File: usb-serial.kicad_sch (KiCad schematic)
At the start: 29 parts, among them J11 Connector, USB-TYPE-C-16P, J3 Connector, USB-TYPE-C-16P, Q8 L8050QLT1G, Q9 L8050QLT1G, U6 CP2102N-Axx-xQFN28

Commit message: fix: corrected 3v3 connections at D5, USB power to LDO, power to I2C expansion
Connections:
- net USB_5V is gone; now on net +5V: C11.1, D5.1 (K)
- net USB2_5V renamed +5V
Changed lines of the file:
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@@
 	(wire
 		(pts
-			(xy 119.38 104.14) (xy 119.38 107.95)
+			(xy 119.38 102.87) (xy 119.38 107.95)
 		)
 		(stroke
@@
 	)
 	(symbol
-		(lib_id "power:VBUS")
-		(at 120.65 34.29 0)
-		(unit 1)
-		(body_style 1)
-		(exclude_from_sim no)
-		(in_bom yes)
-		(on_board yes)
-		(in_pos_files yes)
-		(dnp no)
-		(fields_autoplaced yes)
-		(property "Reference" "#PWR050"
-			(at 120.65 38.1 0)
-			(hide yes)
-			(show_name no)
-			(do_not_autoplace no)
-			(effects
-				(font
-					(size 1.27 1.27)
-				)
-			)
-		)
-		(property "Value" "USB_5V"
-			(at 120.65 29.21 0)
-			(show_name no)
-			(do_not_autoplace no)
-			(effects
-				(font
-					(size 1.27 1.27)
-				)
-			)
-		)
-		(property "Footprint" ""
-			(at 120.65 34.29 0)
-			(hide yes)
-			(show_name no)
-			(do_not_autoplace no)
-			(effects
-				(font
-					(size 1.27 1.27)
-				)
-			)
-		)
-		(property "Datasheet" ""
-			(at 120.65 34.29 0)
-			(hide yes)
-			(show_name no)
-			(do_not_autoplace no)
-			(effects
-				(font
-					(size 1.27 1.27)
-				)
-			)
-		)
-		(property "Description" "Power symbol creates a global label with name \"VBUS\""
-			(at 120.65 34.29 0)
-			(hide yes)
-			(show_name no)
-			(do_not_autoplace no)
-			(effects
-				(font
-					(size 1.27 1.27)
-				)
-			)
-		)
-		(pin "1"
-		)
-		(instances
-			(project "presstimer"
-				(path "/63494a82-20b5-470b-977d-6a82bfa70174/0171fa45-2753-4764-a2d1-635868f3d686"
-					(reference "#PWR050")
-					(unit 1)
-				)
-			)
-		)
-	)
-	(symbol
 		(lib_id "PCM_JLCPCB-Extended:Connector, USB-TYPE-C-16P")
 		(at 43.18 53.34 0)
@@
 	)
 	(symbol
-		(lib_id "power:VBUS")
-		(at 119.38 104.14 0)
-		(unit 1)
-		(body_style 1)
-		(exclude_from_sim no)
-		(in_bom yes)
-		(on_board yes)
-		(in_pos_files yes)
-		(dnp no)
-		(fields_autoplaced yes)
-		(property "Reference" "#PWR062"
-			(at 119.38 107.95 0)
-			(hide yes)
-			(show_name no)
-			(do_not_autoplace no)
-			(effects
-				(font
-					(size 1.27 1.27)
-				)
-			)
-		)
-		(property "Value" "USB2_5V"
-			(at 119.38 99.06 0)
-			(show_name no)
-			(do_not_autoplace no)
-			(effects
-				(font
-					(size 1.27 1.27)
-				)
-			)
-		)
-		(property "Footprint" ""
-			(at 119.38 104.14 0)
-			(hide yes)
-			(show_name no)
-			(do_not_autoplace no)
-			(effects
-				(font
-					(size 1.27 1.27)
-				)
-			)
-		)
-		(property "Datasheet" ""
-			(at 119.38 104.14 0)
-			(hide yes)
-			(show_name no)
-			(do_not_autoplace no)
-			(effects
-				(font
-					(size 1.27 1.27)
-				)
-			)
-		)
-		(property "Description" "Power symbol creates a global label with name \"VBUS\""
-			(at 119.38 104.14 0)
-			(hide yes)
-			(show_name no)
-			(do_not_autoplace no)
-			(effects
-				(font
-					(size 1.27 1.27)
-				)
-			)
-		)
-		(pin "1"
-		)
-		(instances
-			(project "presstimer"
-				(path "/63494a82-20b5-470b-977d-6a82bfa70174/0171fa45-2753-4764-a2d1-635868f3d686"
-					(reference "#PWR062")
-					(unit 1)
-				)
-			)
-		)
-	)
-	(symbol
 		(lib_id "markus:1N5819HW-7-F")
 		(at 85.09 107.95 0)
@@
 	)
 	(symbol
+		(lib_id "power:+5V")
+		(at 120.65 34.29 0)
+		(unit 1)
+		(body_style 1)
+		(exclude_from_sim no)
+		(in_bom yes)
+		(on_board yes)
+		(in_pos_files yes)
+		(dnp no)
+		(fields_autoplaced yes)
+		(property "Reference" "#PWR018"
+			(at 120.65 38.1 0)
+			(hide yes)
+			(show_name no)
+			(do_not_autoplace no)
+			(effects
+				(font
+					(size 1.27 1.27)
+				)
+			)
+		)
+		(property "Value" "+5V"
+			(at 120.65 29.21 0)
+			(show_name no)
+			(do_not_autoplace no)
+			(effects
+				(font
+					(size 1.27 1.27)
+				)
+			)
+		)
+		(property "Footprint" ""
+			(at 120.65 34.29 0)
+			(hide yes)
+			(show_name no)
+			(do_not_autoplace no)
+			(effects
+				(font
+					(size 1.27 1.27)
+				)
+			)
+		)
+		(property "Datasheet" ""
+			(at 120.65 34.29 0)
+			(hide yes)
+			(show_name no)
+			(do_not_autoplace no)
+			(effects
+				(font
+					(size 1.27 1.27)
+				)
+			)
+		)
+		(property "Description" "Power symbol creates a global label with name \"+5V\""
+			(at 120.65 34.29 0)
+			(hide yes)
+			(show_name no)
+			(do_not_autoplace no)
+			(effects
+				(font
+					(size 1.27 1.27)
+				)
+			)
+		)
+		(pin "1"
+		)
+		(instances
+			(project "presstimer"
+				(path "/63494a82-20b5-470b-977d-6a82bfa70174/0171fa45-2753-4764-a2d1-635868f3d686"
+					(reference "#PWR018")
+					(unit 1)
+				)
+			)
+		)
+	)
+	(symbol
 		(lib_id "power:GND")
 		(at 223.52 123.19 0)
@@
 					(unit 1)
 				)
+			)
+		)
+	)
+	(symbol
+		(lib_id "power:+5V")
+		(at 119.38 102.87 0)
+		(unit 1)
+		(body_style 1)
+		(exclude_from_sim no)
+		(in_bom yes)
+		(on_board yes)
+		(in_pos_files yes)
+		(dnp no)
+		(fields_autoplaced yes)
+		(property "Reference" "#PWR019"
+			(at 119.38 106.68 0)
+			(hide yes)
+			(show_name no)
+			(do_not_autoplace no)
+			(effects
+				(font
+					(size 1.27 1.27)
+				)
+			)
+		)
+		(property "Value" "+5V"
+			(at 119.38 97.79 0)
+			(show_name no)
+			(do_not_autoplace no)
+			(effects
+				(font
+					(size 1.27 1.27)
+				)
+			)
+		)
+		(property "Footprint" ""
+			(at 119.38 102.87 0)
+			(hide yes)
+			(show_name no)
+			(do_not_autoplace no)
+			(effects
+				(font
+					(size 1.27 1.27)
+				)
+			)
+		)
+		(property "Datasheet" ""
+			(at 119.38 102.87 0)
+			(hide yes)
+			(show_name no)
+			(do_not_autoplace no)
+			(effects
+				(font
+					(size 1.27 1.27)
+				)
+			)
+		)
+		(property "Description" "Power symbol creates a global label with name \"+5V\""
+			(at 119.38 102.87 0)
+			(hide yes)
+			(show_name no)
+			(do_not_autoplace no)
+			(effects
+				(font
+					(size 1.27 1.27)
+				)
+			)
+		)
+		(pin "1"
+		)
+		(instances
+			(project "presstimer"
+				(path "/63494a82-20b5-470b-977d-6a82bfa70174/0171fa45-2753-4764-a2d1-635868f3d686"
+					(reference "#PWR019")
+					(unit 1)
+				)

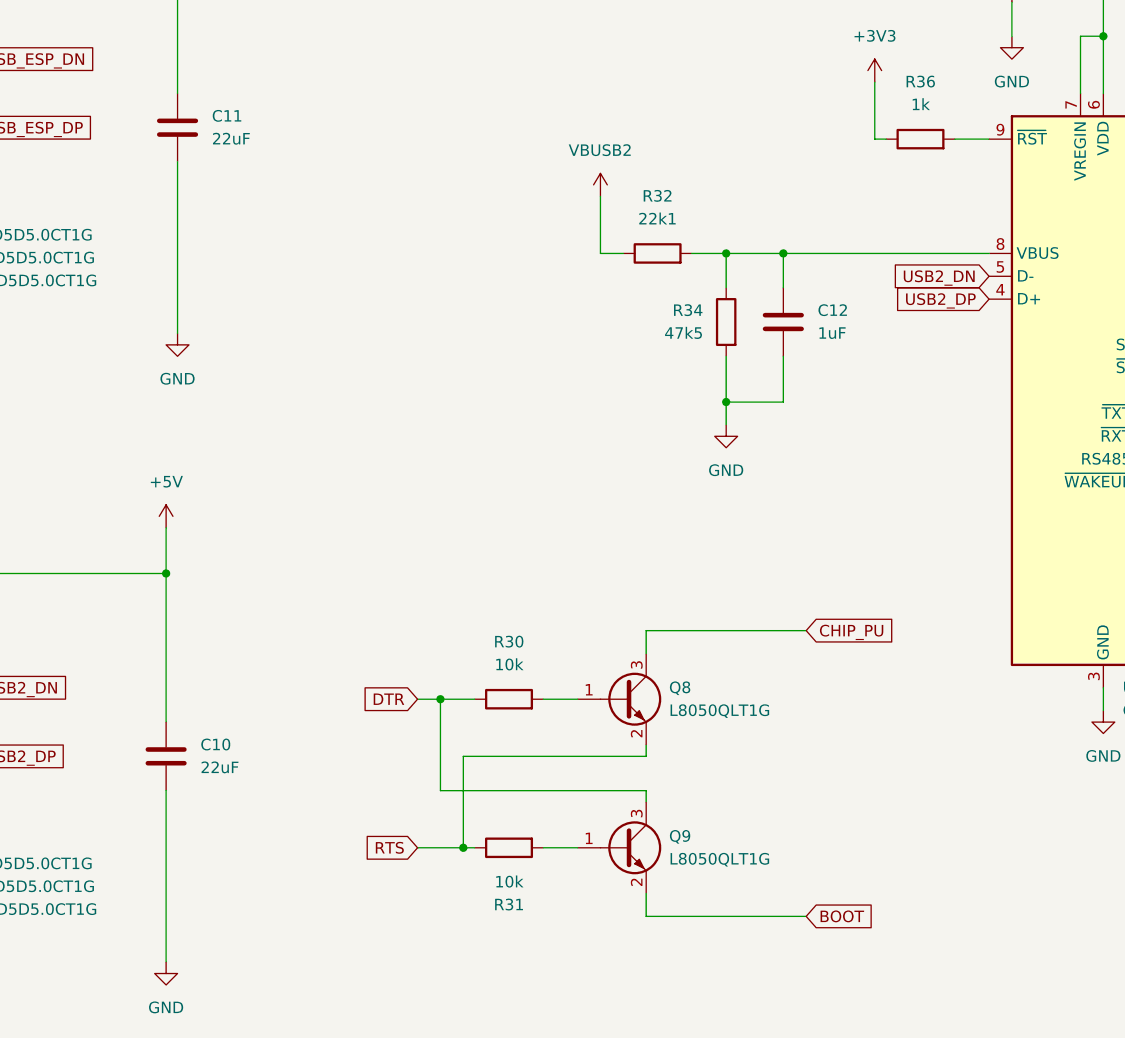
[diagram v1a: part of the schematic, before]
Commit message: fixed ssr pinout
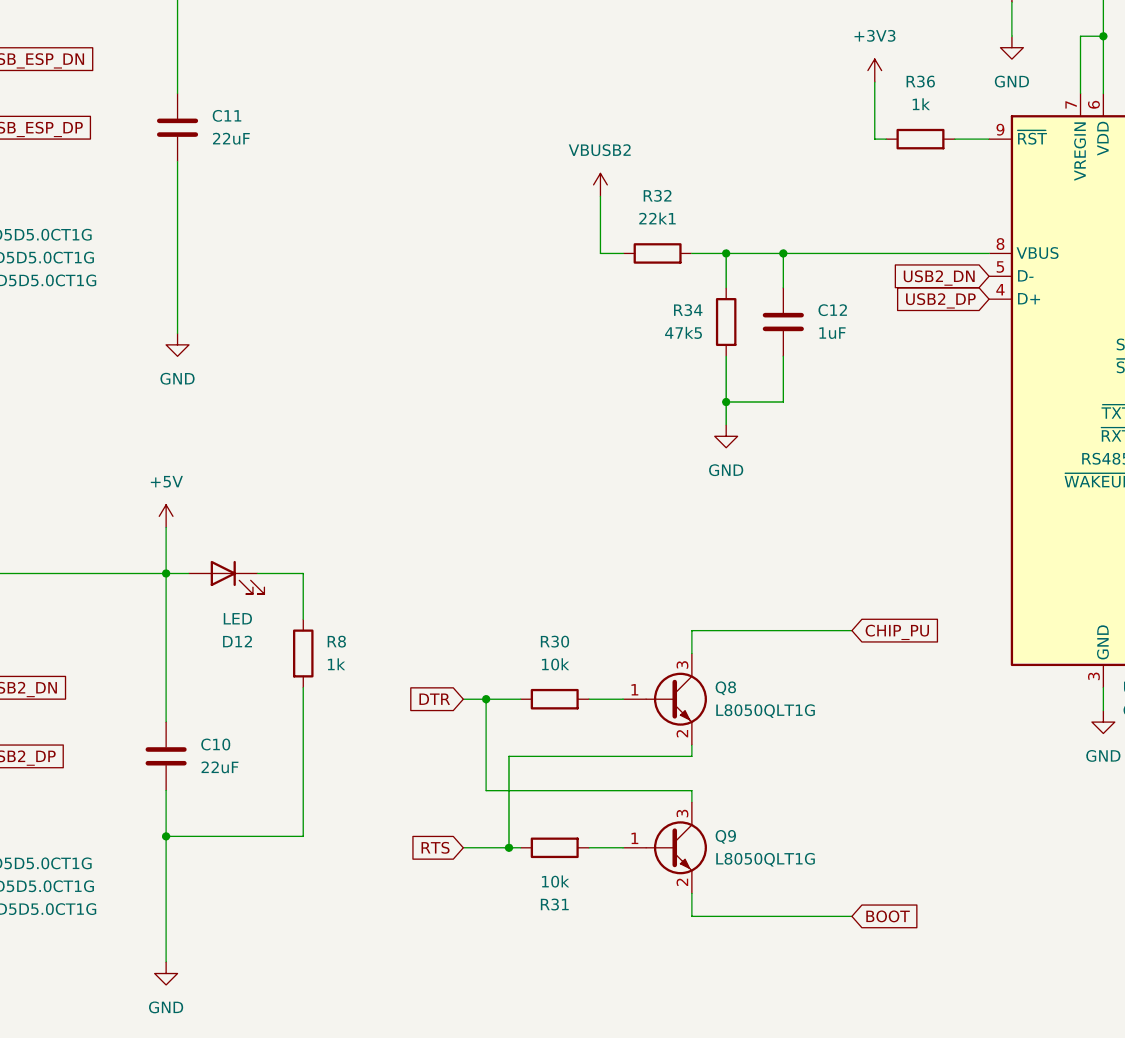
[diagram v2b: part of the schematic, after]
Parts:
- added D12: LED, PCM_JLCPCB:D_0805, symbol Device:LED
- added R8: 1k, PCM_JLCPCB:R_0603, symbol Device:R
- C12, C13, D10, D3, D4, D5, D6, D7, D8, D9: now in the parts list
- J11, J3: now left out of the parts list
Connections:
- net +5V: now also D12.2 (A)
- net GND: now also R8.2
- new net: D12.1 (K), R8.1
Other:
- moved on the sheet: Q8, Q9, R30, R31

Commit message: add: connector heating SSR
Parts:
- removed D12: LED, PCM_JLCPCB:D_0805, symbol Device:LED
- removed R37: 10k, PCM_JLCPCB:R_0603, symbol Device:R
- removed R8: 1k, PCM_JLCPCB:R_0603, symbol Device:R
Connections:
- no-connect marks 19 -> 20
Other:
- moved on the sheet: C12, C13, Q8, Q9, R30, R31, R32, R34, R36, R38, R39, U6
